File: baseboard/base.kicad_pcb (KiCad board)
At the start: 2 copper layers, 180 x 45 mm, 45 parts, among them J1 Conn_02x05_Odd_Even, J2 Barrel_Jack, J3 Barrel_Jack, J4 Conn_01x03_Male, Q1 BSS138, Q2 BSS138, Q3 BSS138, Q4 BSS138, Q5 BSS138, Q6 BSS138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

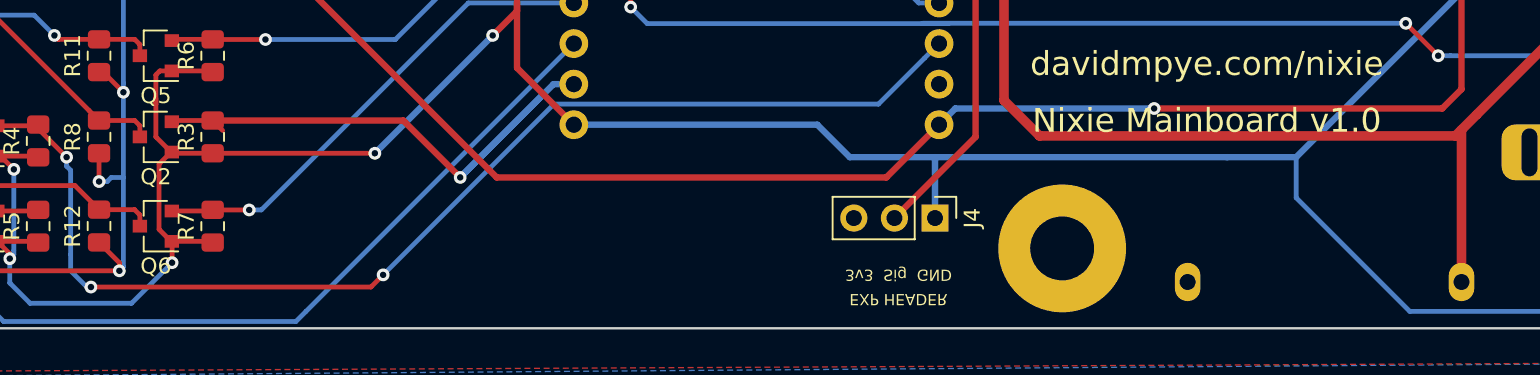
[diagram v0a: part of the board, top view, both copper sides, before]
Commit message: Fix LED level shifter - should be to +5V, not +12V...
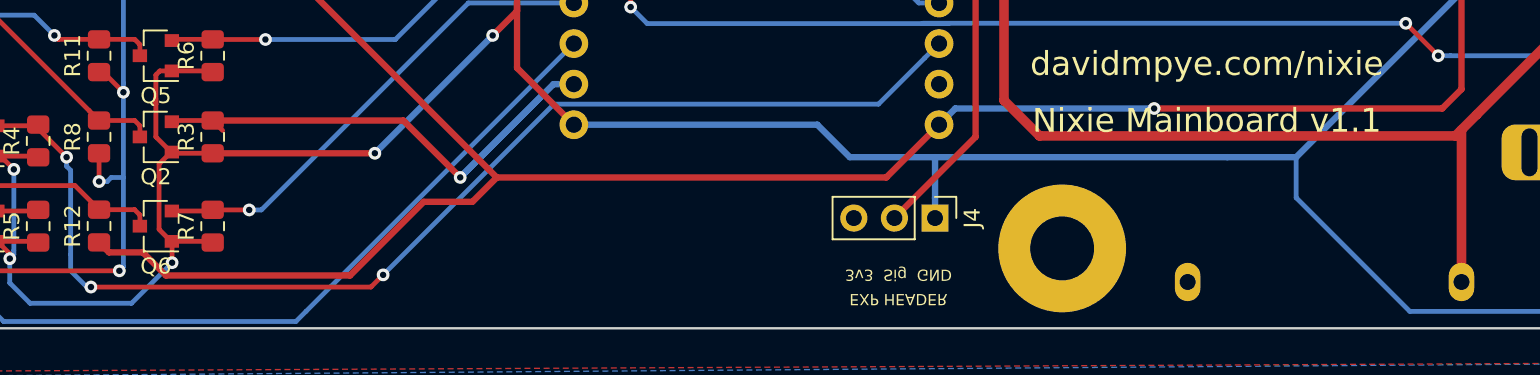
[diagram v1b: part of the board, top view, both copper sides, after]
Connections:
- R12 pad 1: +12V -> +5V
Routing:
- net +5V: track 144.7 -> 173.0 mm
- net +12V: track 231.3 -> 229.0 mm
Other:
- board text added: "Nixie Mainboard v1.1"
- board text removed: "Nixie Mainboard v1.0"
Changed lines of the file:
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@@
     (thickness 1.6)
     (drawings 22)
-    (tracks 352)
+    (tracks 357)
     (zones 0)
     (modules 45)
@@
   )
   (setup
-    (last_trace_width 0.6)
+    (last_trace_width 0.4)
     (user_trace_width 0.3)
     (user_trace_width 0.4)
@@
     )
     (pad 1 smd roundrect (at -1.025 0 90) (size 1.15 1.4) (layers F.Cu F.Paste F.Mask) (roundrect_rratio 0.217391)
-      (net 7 +12V))
+      (net 16 +5V))
     (pad 2 smd roundrect (at 1.025 0 90) (size 1.15 1.4) (layers F.Cu F.Paste F.Mask) (roundrect_rratio 0.217391)
       (net 3 LED_DIN))
@@
     (effects (font (size 1.5 1.5) (thickness 0.3)) (justify mirror))
   )
-  (gr_text "Nixie Mainboard v1.0" (at 118.11 59.436) (layer F.SilkS)
+  (gr_text "Nixie Mainboard v1.1" (at 118.11 59.436) (layer F.SilkS)
     (effects (font (size 1.5 1.5) (thickness 0.3)))
   )
@@
   (via (at 50.038 68.834) (size 0.8) (drill 0.4) (layers F.Cu B.Cu) (net 7))
   (segment (start 50.292 68.58) (end 50.038 68.834) (width 0.3) (layer B.Cu) (net 7))
-  (segment (start 50.038 68.326) (end 48.768 67.056) (width 0.3) (layer F.Cu) (net 7))
-  (segment (start 50.038 68.834) (end 50.038 68.326) (width 0.3) (layer F.Cu) (net 7))
   (segment (start 50.292 62.992) (end 49.53 62.992) (width 0.3) (layer B.Cu) (net 7))
   (segment (start 50.292 62.992) (end 50.292 68.58) (width 0.3) (layer B.Cu) (net 7))
@@
   (segment (start 123.698 61.722) (end 123.698 64.262) (width 0.3) (layer B.Cu) (net 8))
   (via (at 66.031 61.477) (size 0.8) (drill 0.4) (layers F.Cu B.Cu) (net 8))
-  (segment (start 66.031 61.477) (end 55.88 61.477) (width 0.3) (layer F.Cu) (net 8))
+  (segment (start 66.031 61.477) (end 55.88 61.477) (width 0.4) (layer F.Cu) (net 8))
   (segment (start 119.38 61.722) (end 123.698 61.722) (width 0.4) (layer B.Cu) (net 8))
   (segment (start 78.74 29.718) (end 74.93 33.528) (width 0.4) (layer B.Cu) (net 8))
@@
   (segment (start 102.362 58.674) (end 101.346 59.69) (width 0.4) (layer B.Cu) (net 16))
   (segment (start 114.808 58.674) (end 102.362 58.674) (width 0.4) (layer B.Cu) (net 16))
+  (segment (start 51.50937 67.679372) (end 52.955999 69.126001) (width 0.4) (layer F.Cu) (net 16))
+  (segment (start 52.955999 69.126001) (end 64.477999 69.126001) (width 0.4) (layer F.Cu) (net 16))
+  (segment (start 48.768 67.056) (end 49.391372 67.679372) (width 0.4) (layer F.Cu) (net 16))
+  (segment (start 49.391372 67.679372) (end 51.50937 67.679372) (width 0.4) (layer F.Cu) (net 16))
+  (segment (start 64.477999 69.126001) (end 69.088 64.516) (width 0.4) (layer F.Cu) (net 16))
+  (segment (start 72.136 64.516) (end 73.66 62.992) (width 0.4) (layer F.Cu) (net 16))
+  (segment (start 69.088 64.516) (end 72.136 64.516) (width 0.4) (layer F.Cu) (net 16))
   (segment (start 22.26 44.932) (end 22.26 41.24) (width 0.4) (layer F.Cu) (net 17))
   (segment (start 24.41 39.09) (end 40.938 39.09) (width 0.4) (layer F.Cu) (net 17))

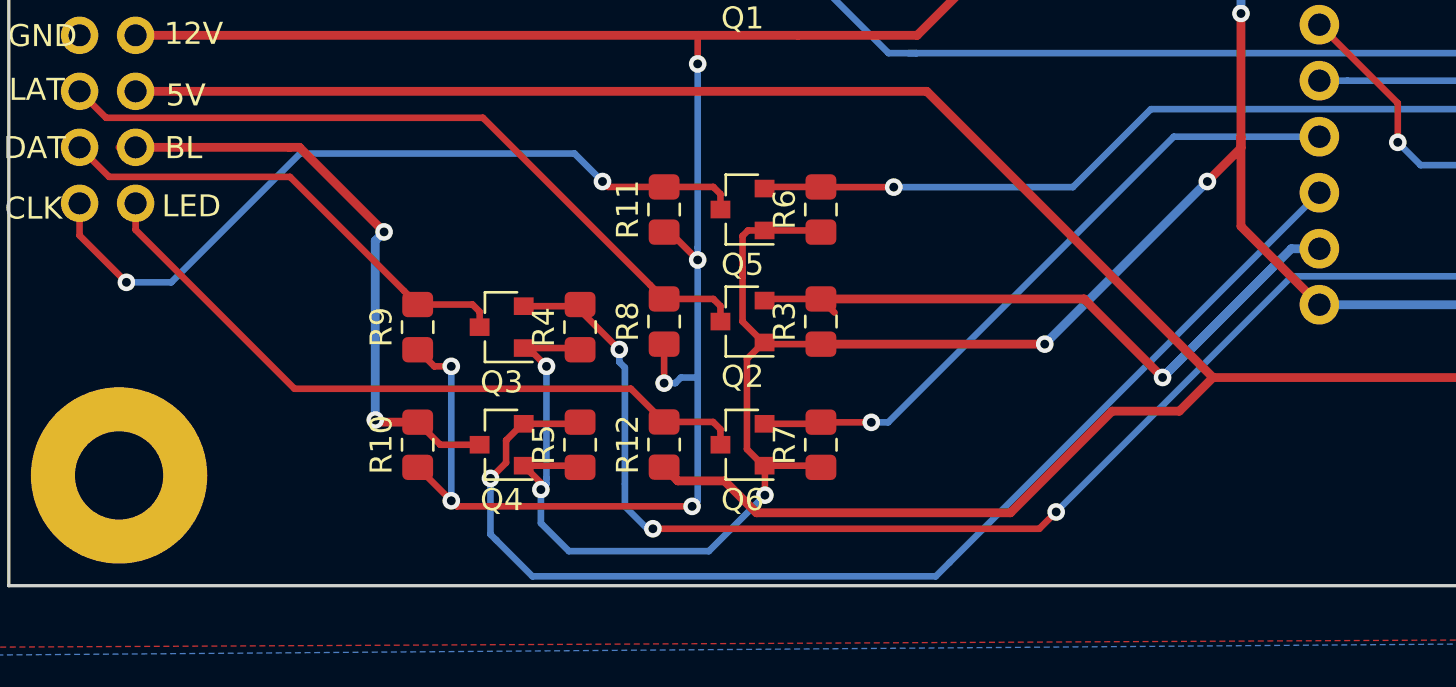
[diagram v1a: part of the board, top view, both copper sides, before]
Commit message: Remove LED level shifter (using diodes on tube 'boards'), so not needed. Rejig GPIOs as wemos won't boot if D8 is pulled HIGH (and the level shifter *did* pull it high)
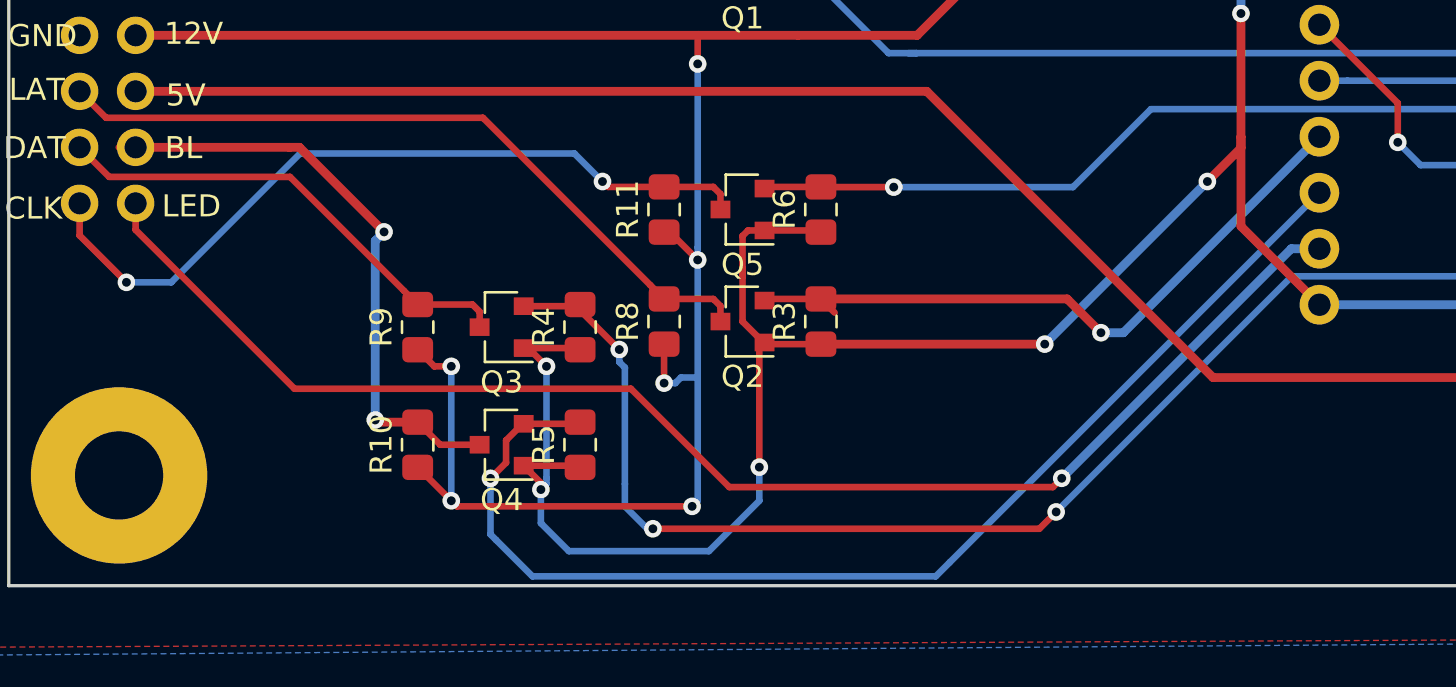
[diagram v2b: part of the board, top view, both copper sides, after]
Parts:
- removed Q6: BSS138, Package_TO_SOT_SMD:SOT-23
- removed R12, R7: 10k, Resistor_SMD:R_0805_2012Metric_Pad1.15x1.40mm_HandSolder
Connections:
- J1 pad 9: LED_DIN -> NEOPIX_3V3
- U1 pad 13: NEOPIX_3V3 -> LATCH
- U1 pad 15: LATCH -> NEOPIX_3V3
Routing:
- net NEOPIX_3V3: track 30.6 -> 64.2 mm
- net LED_DIN: track 32.2 -> 0.00 mm
- net +5V: track 173.0 -> 144.7 mm
- net LATCH: track 37.2 -> 30.4 mm
- net +3V3: track 263.4 -> 260.1 mm

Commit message: Add pullup resistor to switching FET for HVPSU Remove I2C pullups (they aren't needed, as the RTC module has built in pullups)
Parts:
- removed R13, R14: 4k7, Resistor_THT:R_Axial_DIN0309_L9.0mm_D3.2mm_P12.70mm_Horizontal
- added R7: 10K, Resistor_SMD:R_0805_2012Metric_Pad1.15x1.40mm_HandSolder, F.Cu at (58.9, 43.9)
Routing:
- net SCL: track 48.2 -> 75.7 mm
- net SDA: track 49.3 -> 69.8 mm
- net HV_DISABLE: track 52.3 -> 57.0 mm
- net +3V3: track 260.1 -> 264.5 mm, vias 6 -> 7
- net GND: vias 0 -> 1

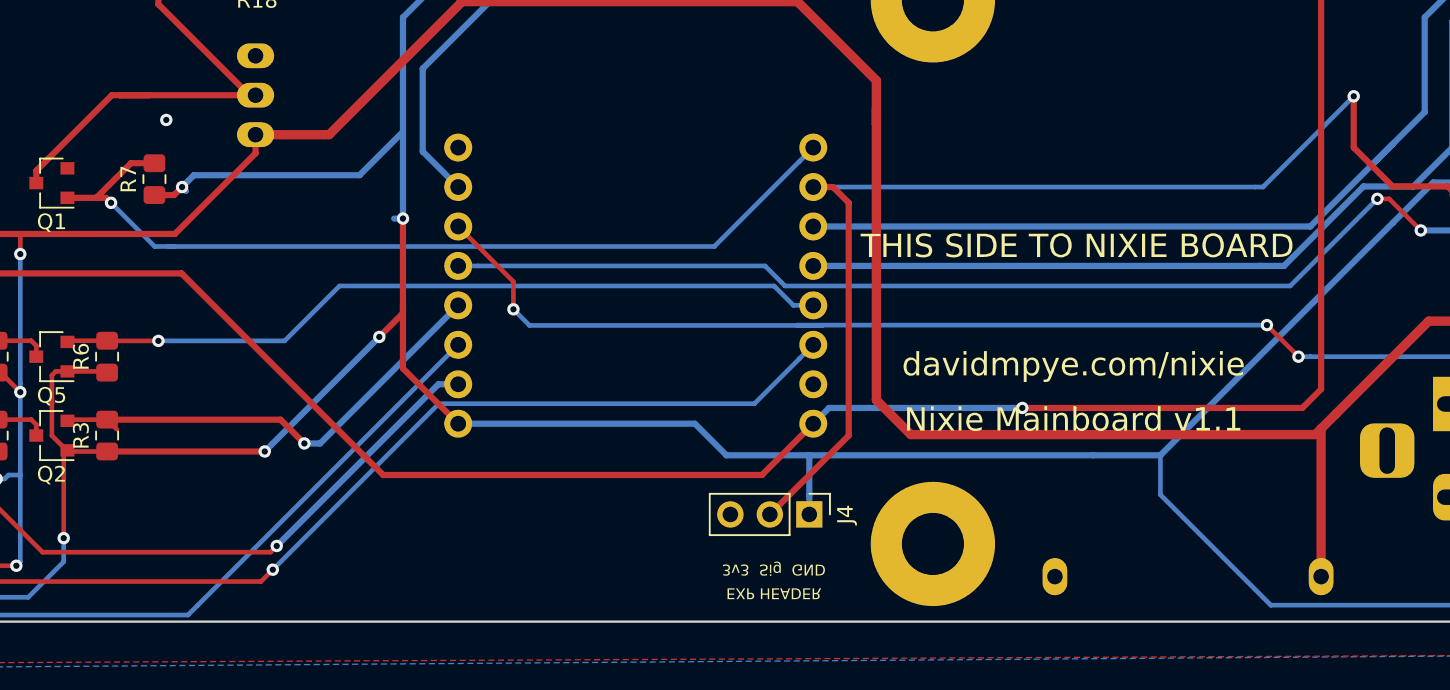
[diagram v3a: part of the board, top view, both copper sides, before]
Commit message: More refactoring of ESP8266 pinout issues to ensure booting functions correctly
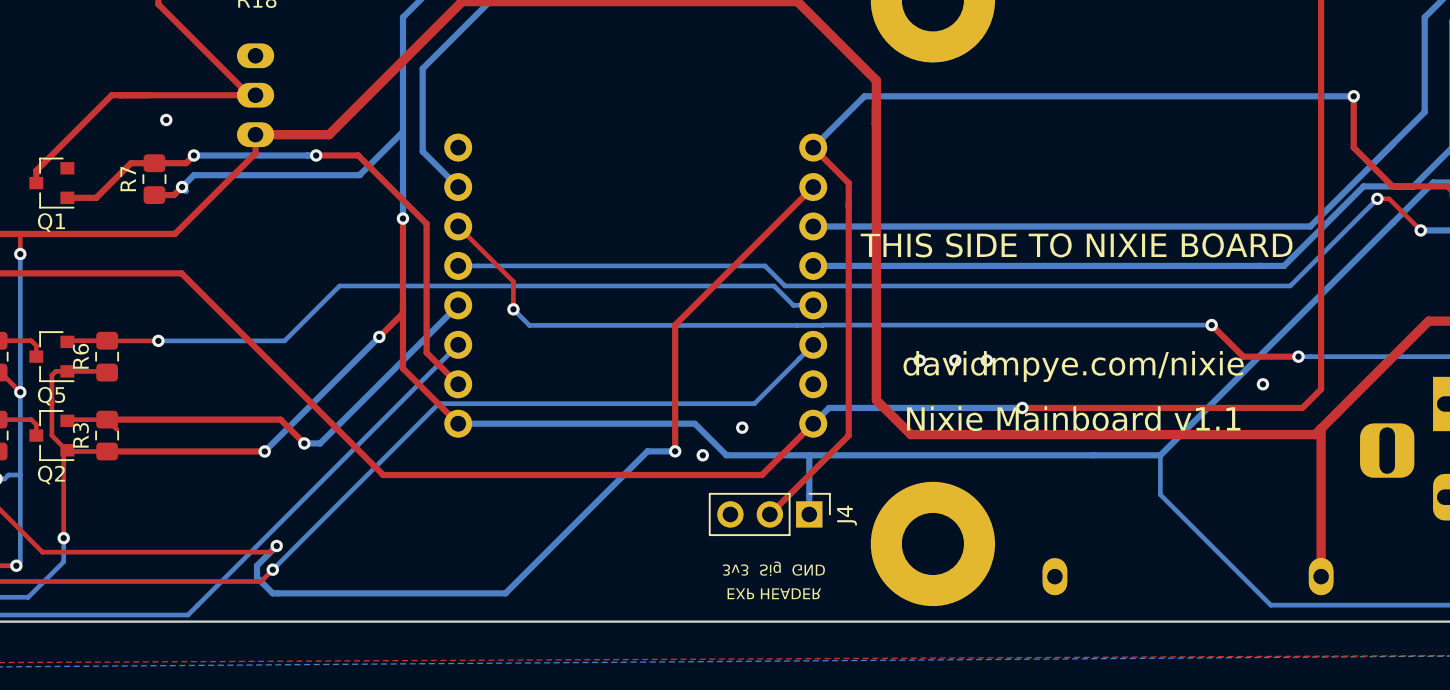
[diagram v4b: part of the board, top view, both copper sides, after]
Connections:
- U1 pad 15: NEOPIX_3V3 -> HV_DISABLE
- U1 pad 7: SW_3 -> NEOPIX_3V3
- U1 pad 8: HV_DISABLE -> SW_3
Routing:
- net NEOPIX_3V3: track 64.2 -> 102.6 mm, vias 1 -> 2
- net HV_DISABLE: track 57.0 -> 37.6 mm, vias 1 -> 2
- net SW_1: track 102.3 -> 101.1 mm
- net SW_3: track 136.6 -> 137.6 mm
- net +3V3: track 264.5 -> 263.9 mm
- net GND: vias 1 -> 7

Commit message: Fix pulldown
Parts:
- turned R7 to 270 degrees
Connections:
- R7 pad 1: +3V3 -> HV_DISABLE
- R7 pad 2: HV_DISABLE -> GND
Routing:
- net +3V3: track 263.9 -> 245.9 mm, vias 7 -> 6
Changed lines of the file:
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@@
     (thickness 1.6)
     (drawings 22)
-    (tracks 375)
+    (tracks 367)
     (zones 0)
     (modules 41)
@@
   )
   (setup
-    (last_trace_width 0.3)
+    (last_trace_width 0.25)
     (user_trace_width 0.3)
     (user_trace_width 0.4)
@@
   )
   (module Resistor_SMD:R_0805_2012Metric_Pad1.15x1.40mm_HandSolder (layer F.Cu)
-    (at 58.928 43.942 90)
+    (at 58.928 43.942 270)
     (descr "Resistor SMD 0805 (2012 Metric), square (rectangular) end terminal, IPC_7351 nominal with elongated pad for handsoldering. (Body size source: https://docs.google.com/spreadsheets/d/1BsfQQcO9C6DZCsRaXUlFlo91Tg2WpOkGARC1WS5S8t0/edit?usp=sharing), generated with kicad-footprint-generator")
     (tags "resistor handsolder")
@@
     (fp_line (start 1.85 -0.95) (end 1.85 0.95) (layer F.CrtYd) (width 0.05))
     (fp_line (start 1.85 0.95) (end -1.85 0.95) (layer F.CrtYd) (width 0.05))
-    (fp_text user %R (at 0 0 90) (layer F.Fab)
+    (fp_text user %R (at 0 0 270) (layer F.Fab)
       (effects (font (size 0.5 0.5) (thickness 0.08)))
     )
-    (pad 1 smd roundrect (at -1.025 0 90) (size 1.15 1.4) (layers F.Cu F.Paste F.Mask) (roundrect_rratio 0.217391)
-      (net 7 +3V3))
-    (pad 2 smd roundrect (at 1.025 0 90) (size 1.15 1.4) (layers F.Cu F.Paste F.Mask) (roundrect_rratio 0.217391)
+    (pad 1 smd roundrect (at -1.025 0 270) (size 1.15 1.4) (layers F.Cu F.Paste F.Mask) (roundrect_rratio 0.217391)
       (net 23 HV_DISABLE))
+    (pad 2 smd roundrect (at 1.025 0 270) (size 1.15 1.4) (layers F.Cu F.Paste F.Mask) (roundrect_rratio 0.217391)
+      (net 1 GND))
     (model ${KISYS3DMOD}/Resistor_SMD.3dshapes/R_0805_2012Metric.wrl
       (at (xyz 0 0 0))
@@
   (segment (start 53.086 61.64) (end 53.324 61.402) (width 0.3) (layer F.Cu) (net 7))
   (segment (start 53.086 67.056) (end 53.086 61.64) (width 0.3) (layer F.Cu) (net 7))
-  (via (at 60.706 44.45) (size 0.8) (drill 0.4) (layers F.Cu B.Cu) (net 7))
-  (segment (start 60.96 44.704) (end 60.706 44.45) (width 0.4) (layer B.Cu) (net 7))
-  (segment (start 59.728 44.967) (end 58.928 44.967) (width 0.4) (layer F.Cu) (net 7))
-  (segment (start 60.189 44.967) (end 59.728 44.967) (width 0.4) (layer F.Cu) (net 7))
-  (segment (start 60.706 44.45) (end 60.189 44.967) (width 0.4) (layer F.Cu) (net 7))
-  (segment (start 61.468 43.688) (end 60.706 44.45) (width 0.4) (layer B.Cu) (net 7))
   (segment (start 74.93 43.688) (end 74.93 46.482) (width 0.4) (layer B.Cu) (net 7))
-  (segment (start 61.468 43.688) (end 72.136 43.688) (width 0.4) (layer B.Cu) (net 7))
   (segment (start 74.93 33.528) (end 74.93 40.894) (width 0.4) (layer B.Cu) (net 7))
-  (segment (start 72.136 43.688) (end 74.93 40.894) (width 0.4) (layer B.Cu) (net 7))
   (segment (start 74.93 40.894) (end 74.93 43.688) (width 0.4) (layer B.Cu) (net 7))
   (segment (start 53.399 59.427) (end 53.324 59.502) (width 0.3) (layer F.Cu) (net 8))
@@
   (segment (start 58.683 42.672) (end 58.928 42.917) (width 0.4) (layer F.Cu) (net 23))
   (segment (start 69.342 42.418) (end 68.776315 42.418) (width 0.4) (layer B.Cu) (net 23))
+  (segment (start 68.776315 42.418) (end 61.468 42.418) (width 0.4) (layer B.Cu) (net 23))
   (via (at 61.468 42.418) (size 0.8) (drill 0.4) (layers F.Cu B.Cu) (net 23))
-  (segment (start 68.776315 42.418) (end 61.468 42.418) (width 0.4) (layer B.Cu) (net 23))
+  (segment (start 58.928 42.917) (end 60.969 42.917) (width 0.4) (layer F.Cu) (net 23))
   (segment (start 60.969 42.917) (end 61.468 42.418) (width 0.4) (layer F.Cu) (net 23))
-  (segment (start 58.928 42.917) (end 60.969 42.917) (width 0.4) (layer F.Cu) (net 23))
   (segment (start 65.038 38.54) (end 65.438 38.54) (width 0.4) (layer F.Cu) (net 30))
   (segment (start 59.182 32.684) (end 65.038 38.54) (width 0.4) (layer F.Cu) (net 30))
